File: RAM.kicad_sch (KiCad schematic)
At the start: 11 parts, among them U43 74LS244

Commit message: motherboard: Fixed a pile of resistor network issues, and concluded initial routing of the CPU and audio amp passives
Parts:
- RN26, RN27: symbol Device:R_Pack04 -> dragonmux:R_Pack04_OddEven
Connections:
- net +5V: now also RN26.5 (R4.2), RN26.7 (R2.2), RN27.5 (R4.2), RN27.7 (R2.2); no longer RN26.2 (R2.1), RN26.4 (R4.1), RN27.2 (R2.1), RN27.4 (R4.1)
- net at JP8.2 (B), U43.8 (I3a): now also RN26.8 (R1.2); no longer RN26.5 (R4.2)
- net at JP10.2 (B), U43.17 (I3b): now also RN27.8 (R1.2); no longer RN27.5 (R4.2)
- net at JP7.2 (B), U43.4 (I1a): now also RN26.4 (R4.1); no longer RN26.7 (R2.2)
- net at JP5.2 (B), U43.11 (I0b): now also RN27.2 (R2.1); no longer RN27.8 (R1.2)
- net at JP9.2 (B), U43.13 (I1b): now also RN27.4 (R4.1); no longer RN27.7 (R2.2)
- net at JP3.2 (B), U43.2 (I0a): now also RN26.2 (R2.1); no longer RN26.8 (R1.2)
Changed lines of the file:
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@@
 	)
 	(symbol
-		(lib_id "Device:R_Pack04")
+		(lib_id "dragonmux:R_Pack04_OddEven")
 		(at 68.58 132.08 180)
 		(unit 1)
@@
 		)
 		(property "Description" "4 resistor network, parallel topology"
-			(at 68.58 132.08 0)
+			(at 69.85 119.38 0)
 			(effects
 				(font
@@
 	)
 	(symbol
-		(lib_id "Device:R_Pack04")
+		(lib_id "dragonmux:R_Pack04_OddEven")
 		(at 58.42 132.08 180)
 		(unit 1)
@@
 		)
 		(property "Description" "4 resistor network, parallel topology"
-			(at 58.42 132.08 0)
-			(effects
-				(font
+			(at 59.69 119.38 0)
+			(effects
+				(font

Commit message: motherboard: Added packaging and ordering information for many of the 7400 logic parts and the DACs
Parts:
- U43: value 74LS244 -> 74HC244; footprint (none) -> Package_SO:SO-20_12.8x7.5mm_P1.27mm; MFR (none) -> Nexperia; MPN (none) -> 74HC244D,653; OC_FARNELL (none) -> 1201322
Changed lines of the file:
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@@
 			)
 		)
-		(property "Value" "74LS244"
+		(property "Value" "74HC244"
 			(at 81.28 168.91 0)
 			(effects
@@
 			)
 		)
-		(property "Footprint" ""
+		(property "Footprint" "Package_SO:SO-20_12.8x7.5mm_P1.27mm"
 			(at 88.9 152.4 0)
 			(effects
@@
 			)
 		)
-		(property "Datasheet" "http://www.ti.com/lit/ds/symlink/sn74ls244.pdf"
+		(property "Datasheet" "https://assets.nexperia.com/documents/data-sheet/74AHC_AHCT244.pdf"
 			(at 88.9 152.4 0)
 			(effects
@@
 			(at 88.9 152.4 0)
 			(effects
+				(font
+					(size 1.27 1.27)
+				)
+				(hide yes)
+			)
+		)
+		(property "MFR" "Nexperia"
+			(at 88.9 152.4 0)
+			(effects
+				(font
+					(size 1.27 1.27)
+				)
+				(hide yes)
+			)
+		)
+		(property "MPN" "74HC244D,653"
+			(at 88.9 152.4 0)
+			(effects
+				(font
+					(size 1.27 1.27)
+				)
+				(hide yes)
+			)
+		)
+		(property "OC_FARNELL" "1201322"
+			(at 88.9 152.4 0)
+			(effects

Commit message: motherboard: Routed out the bulk of the DAC section and feed latches
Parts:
- U43: footprint Package_SO:SO-20_12.8x7.5mm_P1.27mm -> rhais_package-smd:SO-20_12.8x7.5mm_P1.27mm
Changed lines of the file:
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@@
 			)
 		)
-		(property "Footprint" "Package_SO:SO-20_12.8x7.5mm_P1.27mm"
+		(property "Footprint" "rhais_package-smd:SO-20_12.8x7.5mm_P1.27mm"
 			(at 88.9 152.4 0)
 			(effects

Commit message: motherboard: Added more footprints for parts and refined the serial comms section further
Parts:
- JP10, JP3, JP4, JP5, JP6, JP7, JP8, JP9: footprint (none) -> Jumper:SolderJumper-2_P1.3mm_Open_RoundedPad1.0x1.5mm
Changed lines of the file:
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@@
 			)
 		)
-		(property "Footprint" ""
+		(property "Footprint" "Jumper:SolderJumper-2_P1.3mm_Open_RoundedPad1.0x1.5mm"
 			(at 49.53 147.32 0)
 			(effects
@@
 			)
 		)
-		(property "Footprint" ""
+		(property "Footprint" "Jumper:SolderJumper-2_P1.3mm_Open_RoundedPad1.0x1.5mm"
 			(at 49.53 157.48 0)
 			(effects
@@
 			)
 		)
-		(property "Footprint" ""
+		(property "Footprint" "Jumper:SolderJumper-2_P1.3mm_Open_RoundedPad1.0x1.5mm"
 			(at 49.53 142.24 0)
 			(effects
@@
 			)
 		)
-		(property "Footprint" ""
+		(property "Footprint" "Jumper:SolderJumper-2_P1.3mm_Open_RoundedPad1.0x1.5mm"
 			(at 49.53 154.94 0)
 			(effects
@@
 			)
 		)
-		(property "Footprint" ""
+		(property "Footprint" "Jumper:SolderJumper-2_P1.3mm_Open_RoundedPad1.0x1.5mm"
 			(at 49.53 144.78 0)
 			(effects
@@
 			)
 		)
-		(property "Footprint" ""
+		(property "Footprint" "Jumper:SolderJumper-2_P1.3mm_Open_RoundedPad1.0x1.5mm"
 			(at 49.53 139.7 0)
 			(effects
@@
 			)
 		)
-		(property "Footprint" ""
+		(property "Footprint" "Jumper:SolderJumper-2_P1.3mm_Open_RoundedPad1.0x1.5mm"
 			(at 49.53 152.4 0)
 			(effects
@@
 			)
 		)
-		(property "Footprint" ""
+		(property "Footprint" "Jumper:SolderJumper-2_P1.3mm_Open_RoundedPad1.0x1.5mm"
 			(at 49.53 149.86 0)
 			(effects

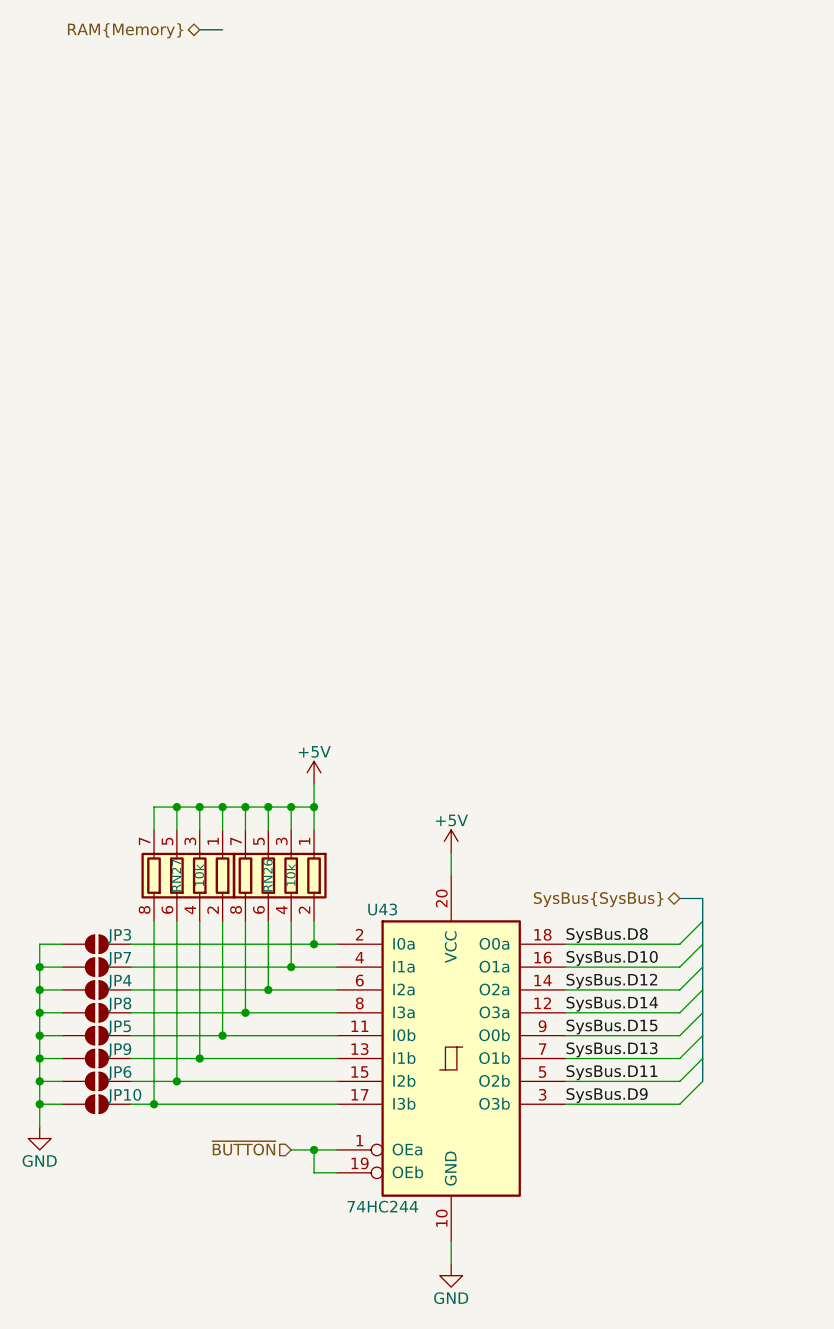
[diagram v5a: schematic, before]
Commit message: motherboard: Mostly routed the ~button signal circuitry
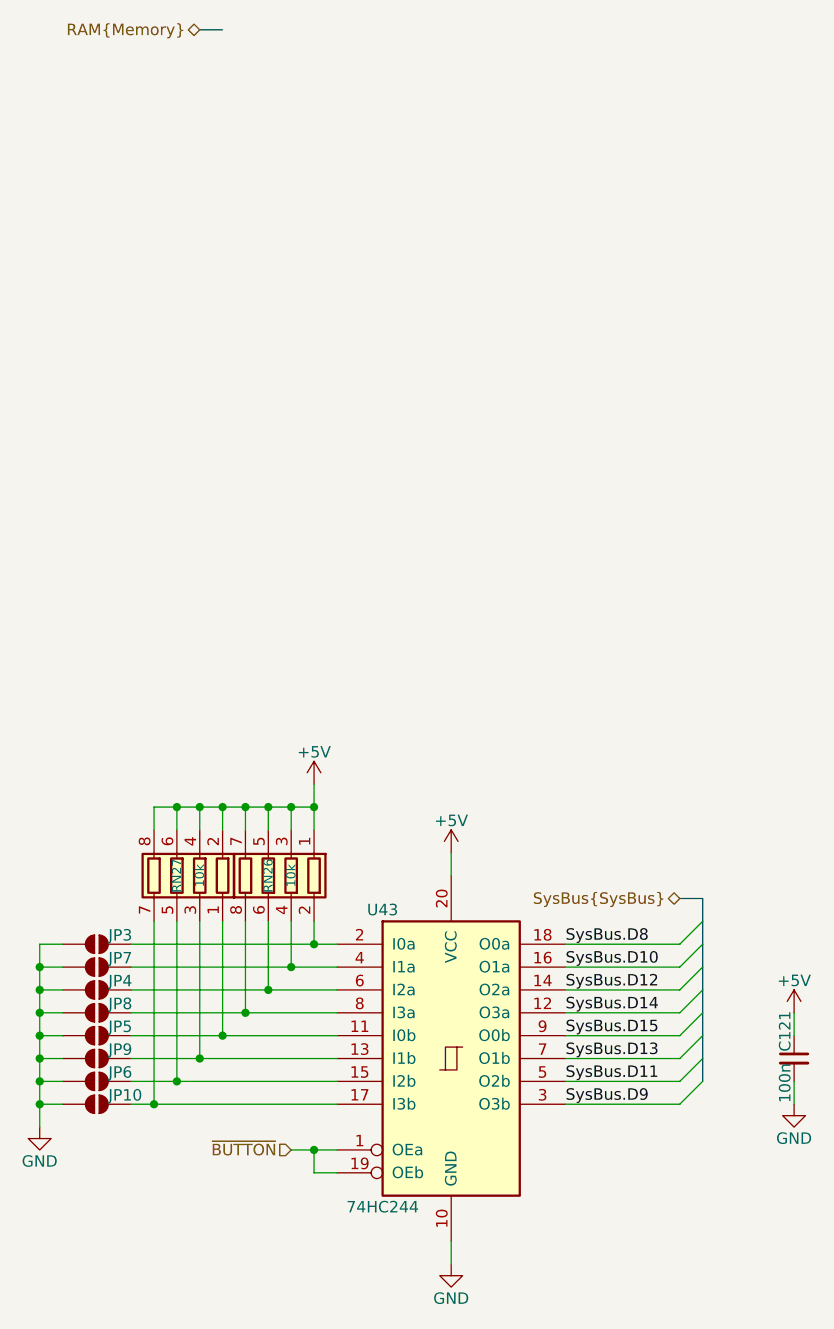
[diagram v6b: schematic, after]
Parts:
- added C121: 100n, rhais_rcl:C0603, symbol Device:C_Small
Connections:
- net +5V: now also RN27.2 (R2.1), RN27.4 (R4.1), RN27.6 (R3.2), RN27.8 (R1.2), C121.1; no longer RN27.1 (R1.1), RN27.3 (R3.1), RN27.5 (R4.2), RN27.7 (R2.2)
- net GND: now also C121.2
- net at JP10.2 (B), U43.17 (I3b): now also RN27.7 (R2.2); no longer RN27.8 (R1.2)
- net at JP5.2 (B), U43.11 (I0b): now also RN27.1 (R1.1); no longer RN27.2 (R2.1)
- net at JP9.2 (B), U43.13 (I1b): now also RN27.3 (R3.1); no longer RN27.4 (R4.1)
- net at JP6.2 (B), U43.15 (I2b): now also RN27.5 (R4.2); no longer RN27.6 (R3.2)
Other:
- moved on the sheet: RN27
